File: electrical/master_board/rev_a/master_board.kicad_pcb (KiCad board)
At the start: 2 copper layers, 145.3 x 156.6 mm, 180 parts, among them CN1 USB3140-30-230-1-C;VERT,2.3FL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, CN10 WOW_OUT;M2x6S, CN2 USB3140-30-230-1-C;VERT,2.3FL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, CN5 LIDAR_ADAPTER;2xF1x3+F1x2, CN6 SERVO;F1x3, CN7 SERVO;F1x3, CN8 SERVO;F1x3, CN81 HCSR04LP;F1X4, CN82 HCSR04LP;F1X4, CN83 HCSR04LP;F1X4, CN84 HCSR04LP;F1X4, CN85 HCSR04LP;F1X4, CN86 HCSR04LP;F1X4, CN87 HCSR04LP;F1X4, CN88 MIKROBUS_MATE;SMALL, CN89 MIKROBUS_MATE;MEDIUM, CN9 SERVO;F1x3, CN90 STADAPTER;F2x4, CN91 HR2_ENCODER;2xF1x3, CN92 HR2_ENCODER;2xF1x3, CN93 POLOLU_U3V70F9;F1x4+F1x5, CN94 RASPI;F2X20, CN95 NUCLEO-F767ZI;2xF2x35, Q1 2N2222;SOT23, Q10 2N7000;SOT23, Q11 2N7000;SOT23, Q12 2N7000;SOT23, Q13 2N7000;SOT23, Q14 2N7000;SOT23, Q15 2N7000;SOT23, Q16 2N7000;SOT23, Q17 2N7000;SOT23, Q18 2N7000;SOT23, Q19 2N7000;SOT23, Q2 POWER_PFET_GSD, Q20 2N7000;SOT23, Q21 PFET_6A_GSD;SOT23, Q22 2N7000;SOT23, Q3 2N2222;SOT23, Q4 2N7000;SOT23, Q5 2N7000;SOT23, Q6 2N7000;SOT23, Q7 2N7000;SOT23, Q8 2N7000;SOT23, Q9 2N7000;SOT23, SW1 BUTTON;6x3.5, SW2 BUTTON;6x3.5, SW3 BUTTON;6x3.5, U1 LM66100;SOT363, U10 CD450B;TTSOP16, U11 SN74HCS595;TTSOP16, U12 SN74HCS595;TTSOP16, U13 74LVC1G11;SOT363, U14 MCP2542;SOIC8, U15 MCP2542;SOIC8, U16 74LVC1G74;TSSOP8, U17 CPC1017N;SOP4W3.8L4.1, U18 CPC1017N;SOP4W3.8L4.1, U2 MCP7940;SOIC8, U3 CAT24C32;SOIC8, U4 DRV8833PWPR;16HTSSOP, U5 SN74HCS595;TTSOP16, U6 SN74HCS166;TTSOP16, U7 SN74HCS166;TTSOP16, U8 SN74HCS595;TTSOP16, U9 CD450B;TTSOP16, X1 32.768kHz9pF;3.2x1.5

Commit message: More work on ground planes.
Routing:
- net /GND: track 1408.5 -> 1620.5 mm, vias 95 -> 136
- net /WOW_EN: track 131.5 -> 160.6 mm, vias 2 -> 3
- net /3.3V: track 785.7 -> 795.6 mm
- net /P5V: track 766.9 -> 773.6 mm
- net /5V: track 811.0 -> 817.1 mm
- net /Power/PWR_SW_A: track 271.0 -> 266.8 mm
- net /SERVO1: track 117.1 -> 113.2 mm
- net /LED's/LED2: track 176.4 -> 173.7 mm
- net /RMOTOR_CTL1: track 54.6 -> 51.9 mm
- net /LED's/LED1: track 170.7 -> 168.0 mm
- net /SWDIO: track 187.8 -> 190.4 mm
- net /ECHO7: track 90.4 -> 93.0 mm
- net /Sonars and Servos/TRIG1_5V: track 171.0 -> 173.5 mm, vias 9 -> 11
- net /Power/USB5V: track 57.4 -> 59.7 mm
- net /SWCLK: track 192.4 -> 194.2 mm
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- added copper zone on F.Cu, net /GND
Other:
- outline, holes or cut-outs redrawn

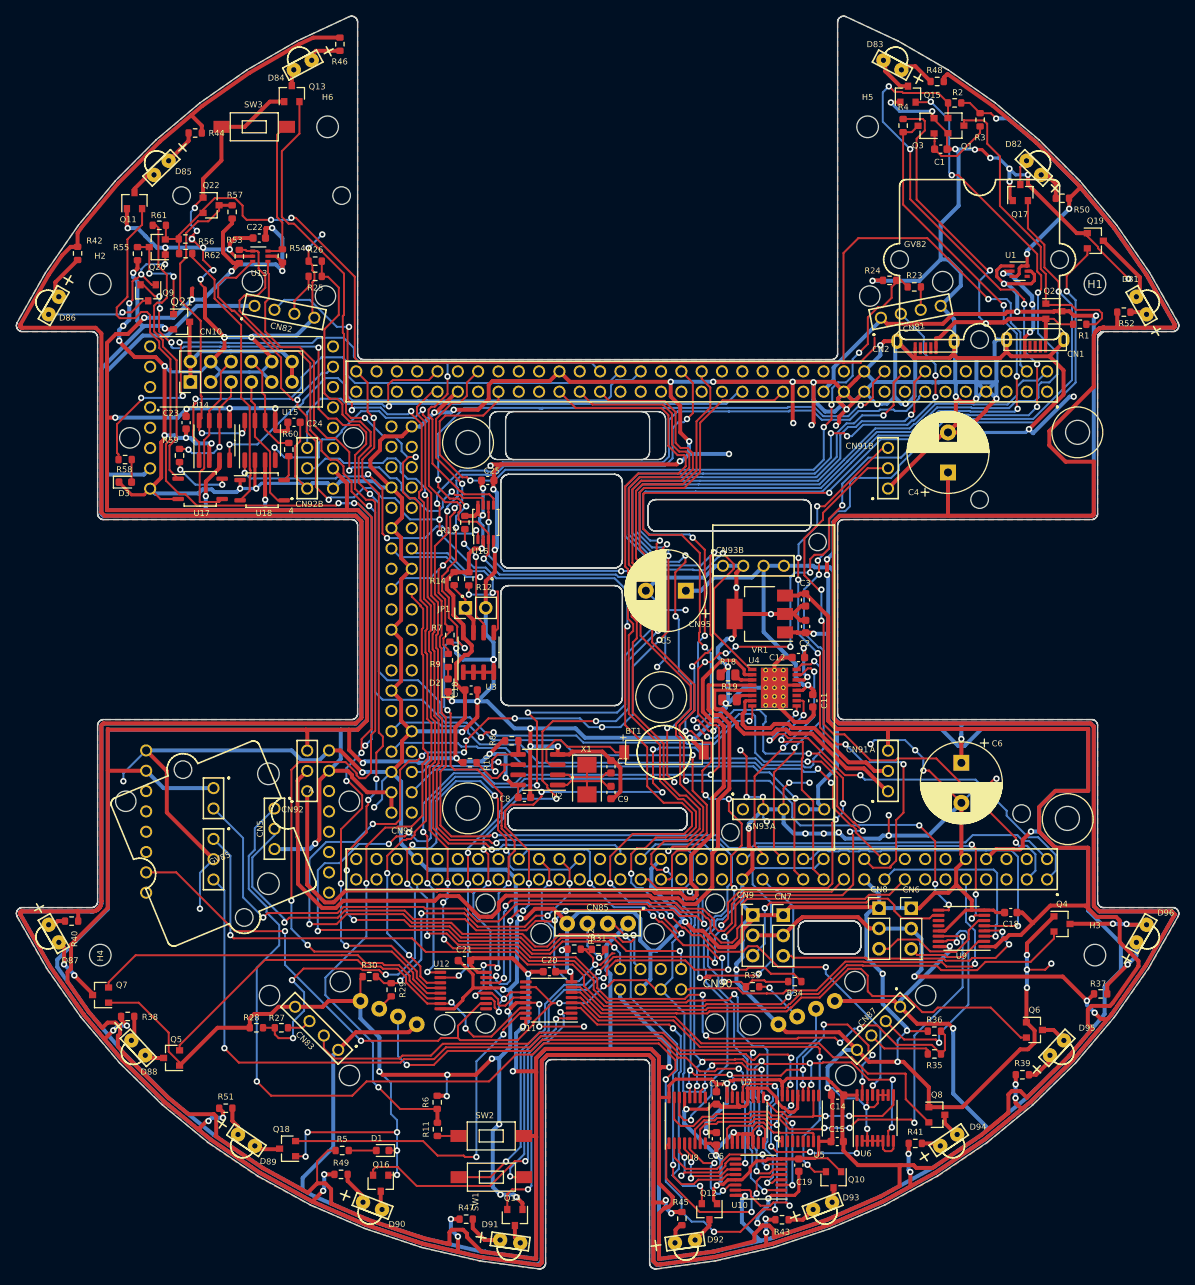
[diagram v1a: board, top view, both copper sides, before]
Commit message: Added power test points/shunt/LED's.
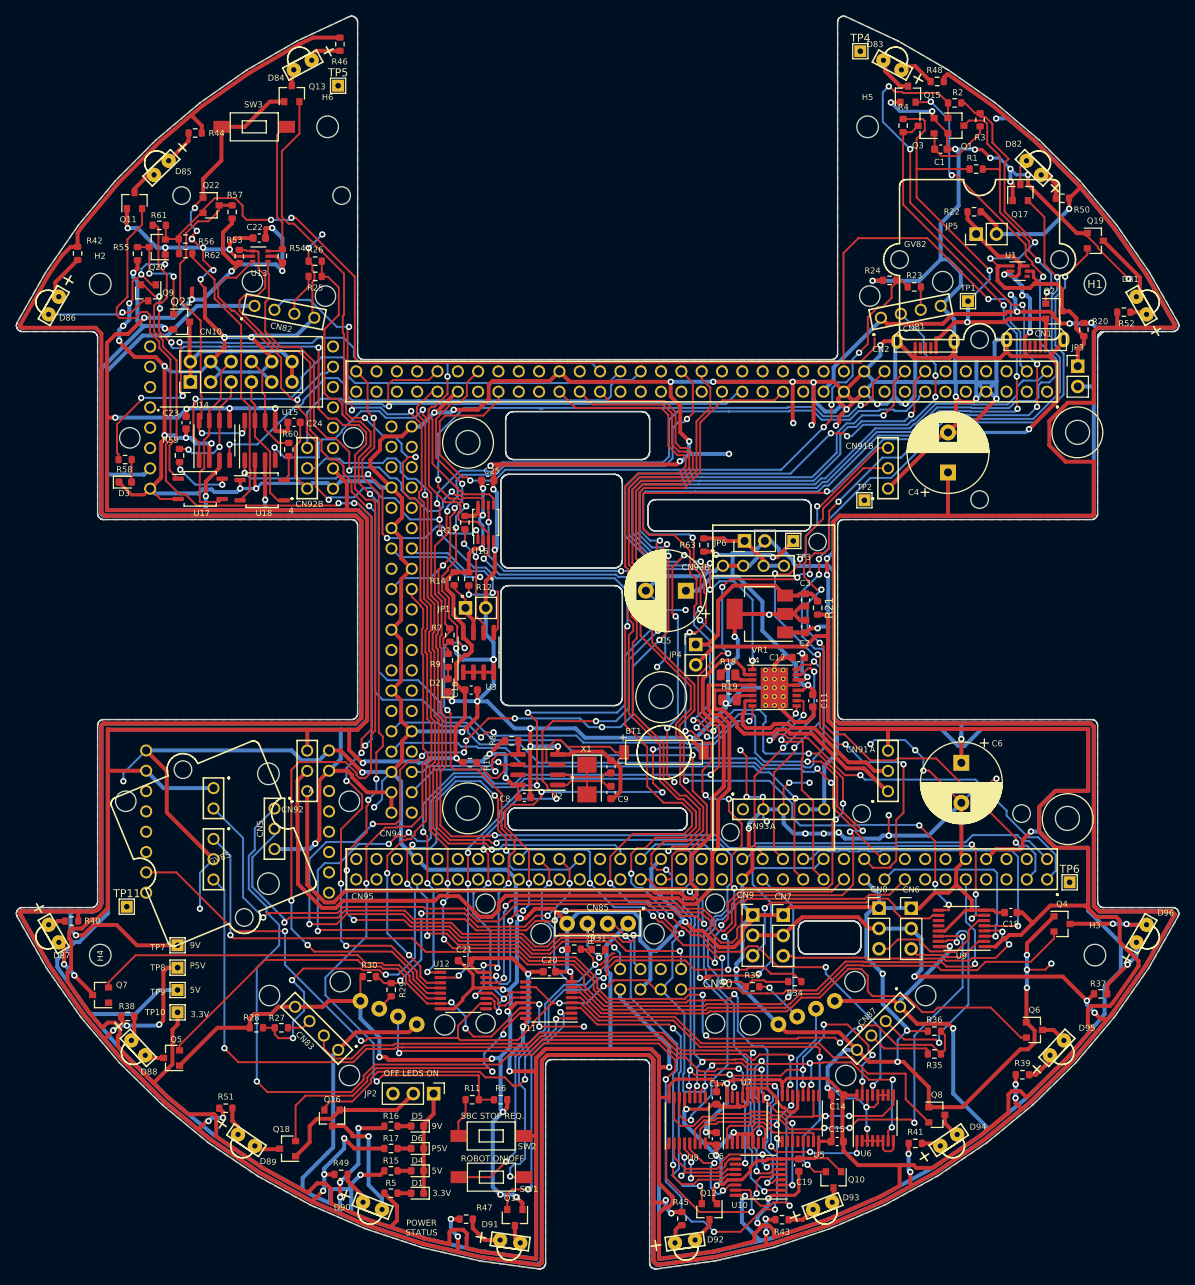
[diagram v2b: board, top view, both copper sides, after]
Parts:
- added D4: LEDGRN;1608, LED_SMD:LED_0603_1608Metric, F.Cu at (77.5, 168.9)
- added D5: LEDGRN;1608, LED_SMD:LED_0603_1608Metric, F.Cu at (77.5, 163.3)
- added D6: LEDGRN;1608, LED_SMD:LED_0603_1608Metric, F.Cu at (77.5, 166.1)
- added JP2: LED_EN;M1x3, Connector_PinHeader_2.54mm:PinHeader_1x03_P2.54mm_Vertical, F.Cu at (79.5, 159.3)
- added JP3: SHUNT;M1x2, Connector_PinHeader_2.54mm:PinHeader_1x02_P2.54mm_Vertical, F.Cu at (160.0, 68.3)
- added JP4: SHUNT;M1x2, Connector_PinHeader_2.54mm:PinHeader_1x02_P2.54mm_Vertical, F.Cu at (112.3, 103.1)
- added JP5: SHUNT;M1x2, Connector_PinHeader_2.54mm:PinHeader_1x02_P2.54mm_Vertical, F.Cu at (147.3, 51.8)
- added JP6: SHUNT;M1x2, Connector_PinHeader_2.54mm:PinHeader_1x02_P2.54mm_Vertical, F.Cu at (118.4, 90.2)
- added R15: 470Ω;1608, Resistor_SMD:R_0603_1608Metric, F.Cu at (74.2, 168.9)
- added R16: 1KΩ;1608, Resistor_SMD:R_0603_1608Metric, F.Cu at (74.2, 163.3)
- added R17: 470Ω;1608, Resistor_SMD:R_0603_1608Metric, F.Cu at (74.2, 166.1)
- added R20: 0Ω;1608, Resistor_SMD:R_0603_1608Metric, F.Cu at (160.8, 63.8)
- added R21: 0Ω;1608, Resistor_SMD:R_0603_1608Metric, F.Cu at (127.5, 98.6)
- added R22: 0Ω;1608, Resistor_SMD:R_0603_1608Metric, F.Cu at (147.1, 49.0)
- added R63: 0Ω;1608, Resistor_SMD:R_0603_1608Metric, F.Cu at (113.3, 90.7)
- added TP1: USB5V, TestPoint:TestPoint_THTPad_1.5x1.5mm_Drill0.7mm, F.Cu at (146.3, 60.2)
- added TP10: 3.3V, TestPoint:TestPoint_THTPad_1.5x1.5mm_Drill0.7mm, F.Cu at (47.5, 149.1)
- added TP11: GND, TestPoint:TestPoint_THTPad_1.5x1.5mm_Drill0.7mm, F.Cu at (41.1, 135.9)
- added TP2: GND, TestPoint:TestPoint_THTPad_1.5x1.5mm_Drill0.7mm, F.Cu at (133.3, 85.1)
- added TP3: GND, TestPoint:TestPoint_THTPad_1.5x1.5mm_Drill0.7mm, F.Cu at (124.5, 90.2)
- added TP4: GND, TestPoint:TestPoint_THTPad_1.5x1.5mm_Drill0.7mm, F.Cu at (132.8, 29.0)
- added TP5: GND, TestPoint:TestPoint_THTPad_1.5x1.5mm_Drill0.7mm, F.Cu at (67.6, 33.3)
- added TP6: GND, TestPoint:TestPoint_THTPad_1.5x1.5mm_Drill0.7mm, F.Cu at (159.0, 132.8)
- added TP7: 9V, TestPoint:TestPoint_THTPad_1.5x1.5mm_Drill0.7mm, F.Cu at (47.5, 140.7)
- added TP8: P5V, TestPoint:TestPoint_THTPad_1.5x1.5mm_Drill0.7mm, F.Cu at (47.5, 143.5)
- added TP9: 5V, TestPoint:TestPoint_THTPad_1.5x1.5mm_Drill0.7mm, F.Cu at (47.5, 146.3)
- R5: value 470Ω;1608 -> 330Ω;1608
- moved R1 23.3 mm to (147.3, 43.7)
- moved Q16 10.2 mm to (66.8, 162.3)
- moved R5 8.10 mm to (74.2, 171.7)
- moved R6 7.94 mm to (87.9, 160.0), turned to 0 degrees
- moved D1 6.88 mm to (77.5, 171.7)
- moved R11 5.72 mm to (84.3, 160.0), turned to 0 degrees
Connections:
- net /Power/PWR_LED renamed /Power/3.3V_LED
- C3 pad 1: /3.3V -> /Power/SHUNT_3.3
- CN93 pad 8: /9V -> /Power/SHUNT_9V
- CN93 pad 9: /9V -> /Power/SHUNT_9V
- D1 pad 1: /GND -> Net-(D1-Pad1)
- Q2 pad 3: /5V -> /Power/SHUNT_5V
- R2 pad 1: /5V -> /Power/SHUNT_5V
- R3 pad 1: /5V -> /Power/SHUNT_5V
- U1 pad 1: /5V -> /Power/SHUNT_5V
- U1 pad 3: /P5V -> /Power/SHUNT_P5V
- U1 pad 5: /5V -> /Power/SHUNT_5V
- U1 pad 6: /P5V -> /Power/SHUNT_P5V
- VR1 pad 3: /3.3V -> /Power/SHUNT_3.3
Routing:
- net /Power/SHUNT_5V: track 0.00 -> 57.3 mm, vias 0 -> 2
- net /9V: track 521.3 -> 563.1 mm, vias 4 -> 9
- net /GND: track 1620.5 -> 1581.5 mm, vias 136 -> 128
- net /P5V: track 773.6 -> 801.6 mm, vias 21 -> 22
- net /3.3V: track 795.6 -> 820.7 mm
- net /Power/SHUNT_3.3: track 0.00 -> 21.9 mm
- net /Power/SHUNT_P5V: track 0.00 -> 13.6 mm
- net Net-(D1-Pad1): track 0.00 -> 13.0 mm
- net Net-(D90-Pad1): track 2.75 -> 15.1 mm, vias 0 -> 1
- net /Power/SHUNT_9V: track 0.00 -> 11.8 mm
- net /Power/PWR_FET_G: track 39.7 -> 31.6 mm, vias 0 -> 2
- net /Single Board Computer/SBC_STOP: track 83.4 -> 90.3 mm
- net /5V: track 817.1 -> 823.1 mm, vias 14 -> 16
- net /Sonars and Servos/TRIG1_5V: track 173.5 -> 168.2 mm
- net /RQUAD_B: track 71.3 -> 75.3 mm
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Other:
- board text added: "3.3V"
- board text added: "5V"
- board text added: "9V"
- board text added: "OFF LEDS ON"
- board text added: "P5V"
- board text added: "POWER STATUS"
- board text added: "ROBOT ON/OFF"
- board text added: "SBC STOP REQ."

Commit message: More DRC work.
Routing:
- net /GND: track 1581.5 -> 1605.0 mm, vias 128 -> 130

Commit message: Worked on WOWBus TO DO list.
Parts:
- added JP7: EXT_ESTOP;M1x2, Connector_PinHeader_2.54mm:PinHeader_1x02_P2.54mm_Vertical, F.Cu at (58.4, 42.7)
- added JP8: SHUNT;M1x2, Connector_PinHeader_2.54mm:PinHeader_1x02_P2.54mm_Vertical, F.Cu at (51.1, 61.7)
- added R64: 0Ω;1608, Resistor_SMD:R_0603_1608Metric, F.Cu at (51.1, 57.9)
- moved Q21 5.12 mm to (48.3, 57.7)
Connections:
- Q21 pad 3: /WOWBus/WOW_POW_OUT -> Net-(JP8-Pad1)
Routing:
- net Net-(JP8-Pad1): track 0.00 -> 6.84 mm
- net /WOWBus/WOW_POW_OUT: track 24.0 -> 29.2 mm, vias 0 -> 1
- net /WOWBus/~WOW_EN: track 12.7 -> 8.15 mm
- net /~NRST: track 376.7 -> 373.6 mm
- net /WOWBus/WOW_STDBY: track 41.0 -> 43.2 mm
- net /WOWBus/WOW_ESTOP_OPTO: track 34.4 -> 36.1 mm
- net /3.3V: track 820.7 -> 819.2 mm, vias 24 -> 23
- net /LED's/LED6: track 142.2 -> 143.7 mm
- net /WOWBus/WOW_COM_OPTO: track 35.6 -> 34.3 mm
- net Net-(JP7-Pad1): track 18.1 -> 19.4 mm
- net /~MOTOR_FAULT: track 122.5 -> 121.5 mm
- net /GND: track 1605.0 -> 1605.9 mm, vias 130 -> 129
- net /9V: track 563.1 -> 563.6 mm
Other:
- board text added: "ESTOP TRIG"

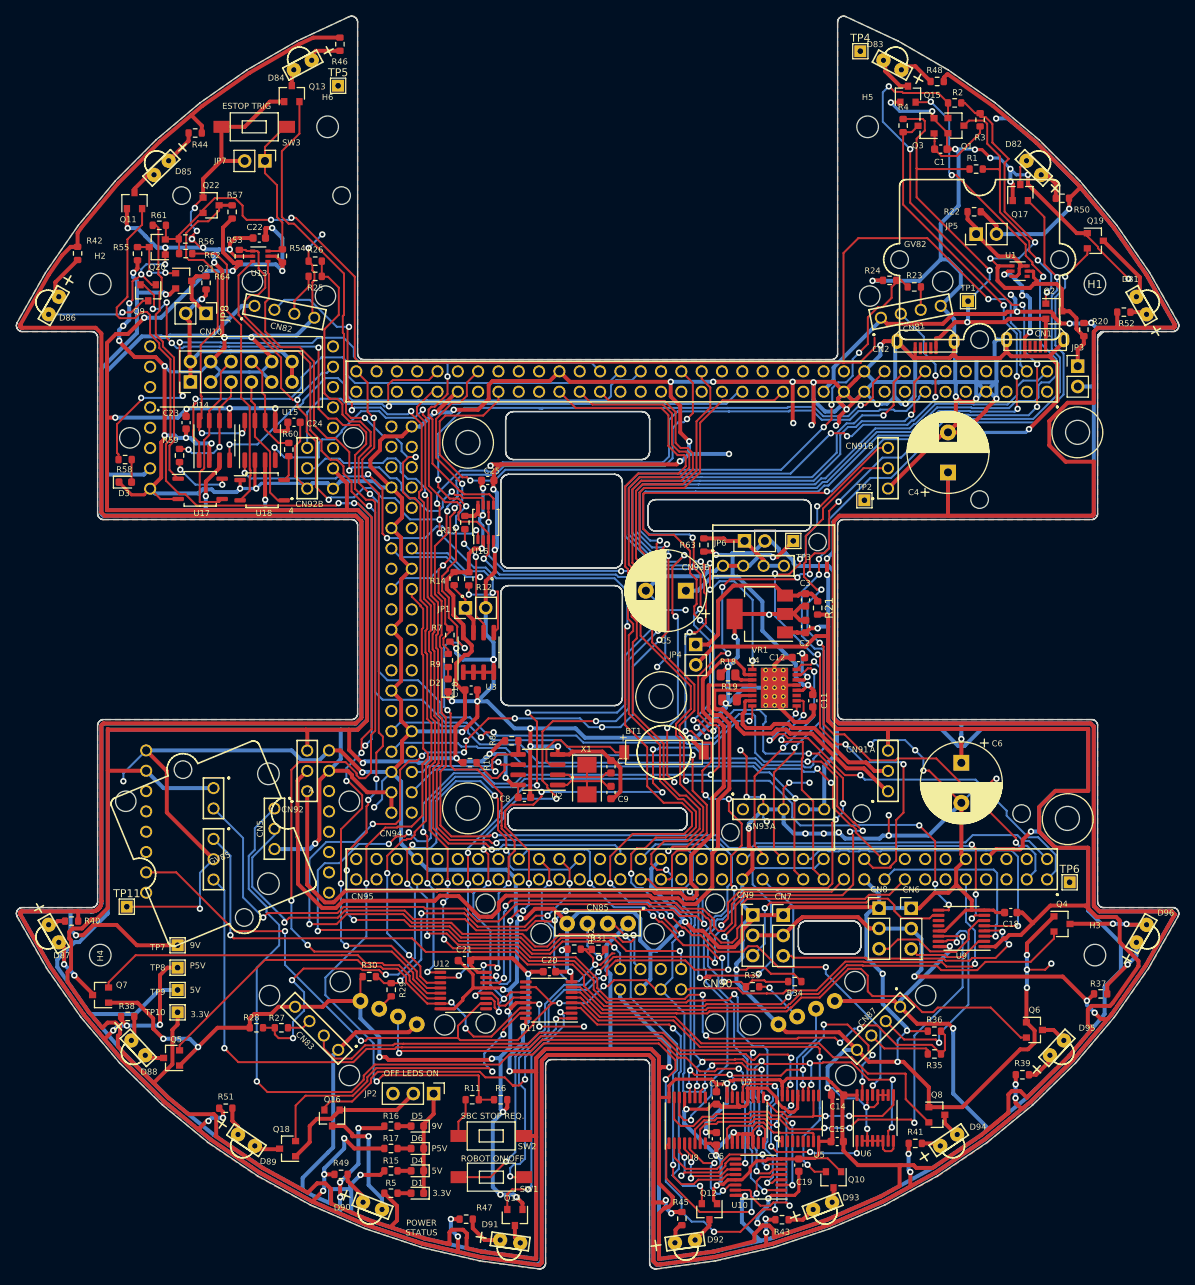
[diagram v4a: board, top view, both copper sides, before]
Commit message: Continuing to add test points.
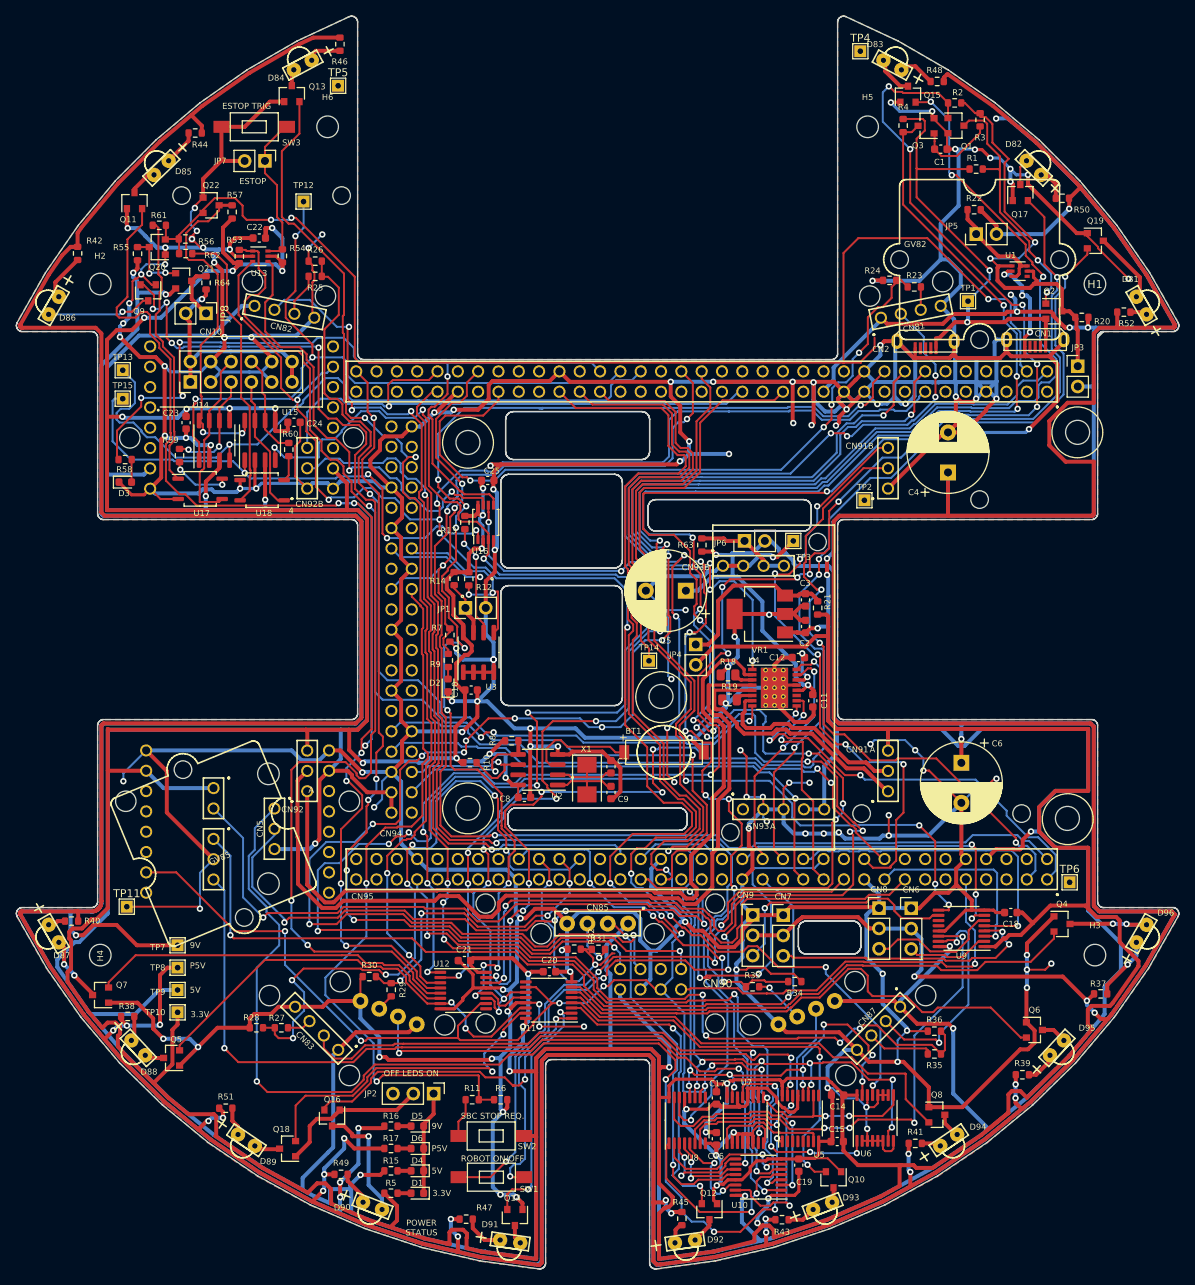
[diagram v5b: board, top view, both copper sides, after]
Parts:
- added TP12: WOW_TX;M1x1, TestPoint:TestPoint_THTPad_1.5x1.5mm_Drill0.7mm, F.Cu at (63.2, 47.8)
- added TP13: WOW_RX;M1x1, TestPoint:TestPoint_THTPad_1.5x1.5mm_Drill0.7mm, F.Cu at (40.6, 68.8)
- added TP14: ~ESTOP_CLR, TestPoint:TestPoint_THTPad_1.5x1.5mm_Drill0.7mm, F.Cu at (106.4, 105.2)
- added TP15: ESTOP_TRIG;M1x1, TestPoint:TestPoint_THTPad_1.5x1.5mm_Drill0.7mm, F.Cu at (40.6, 72.4)
- moved R20 1.55 mm to (160.5, 62.2), turned to 0 degrees
- moved R63 0.25 mm to (113.0, 90.7)
- moved R22 0.25 mm to (147.1, 48.8)
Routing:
- net /WOW_RX: track 61.0 -> 85.8 mm
- net /WOWBus/ESTOP_TRIG: track 40.1 -> 64.7 mm
- net /WOW_TX: track 67.0 -> 89.5 mm, vias 1 -> 3
- net /~ESTOP_CLR: track 57.7 -> 71.1 mm, vias 3 -> 5
- net /SWDIO: track 190.1 -> 191.6 mm
- net /LEDS_SCLK: track 154.3 -> 155.3 mm
- net /GND: track 1605.9 -> 1606.6 mm
- net /Power/SHUNT_5V: track 57.3 -> 56.7 mm
- net /LED's/LED3: track 186.1 -> 186.6 mm
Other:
- board text added: "ESTOP"
